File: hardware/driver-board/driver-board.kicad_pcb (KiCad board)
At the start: 4 copper layers, 42.2 x 36.8 mm, 57 parts, among them J1 Conn_01x13_Male, U1 TXS0108E, U2 ME6210, U3 ME6210, U4 TLV61046ADB, U5 NC7SZ125, U6 FT813, U7 ER-TFT040-2, X1 YSX321SL

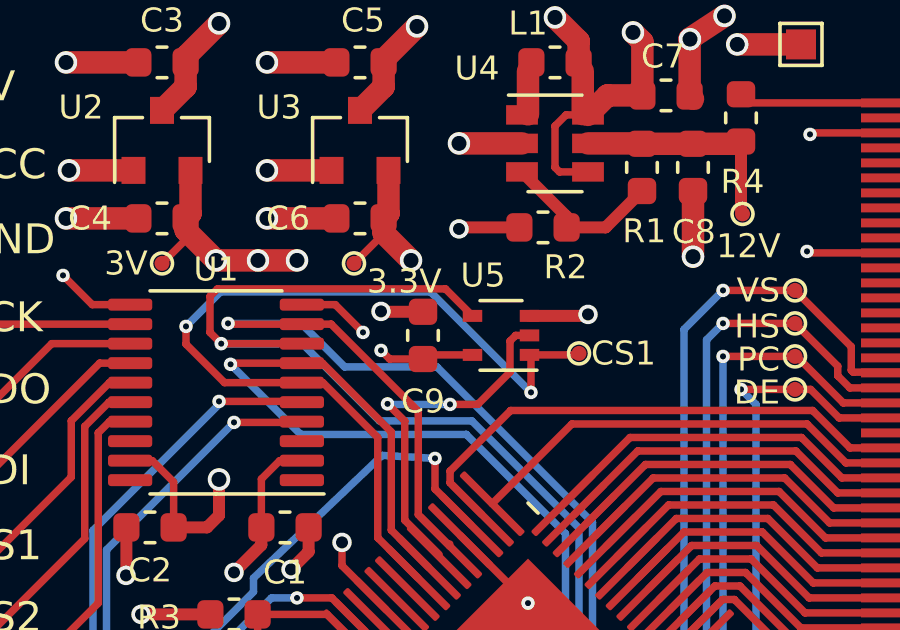
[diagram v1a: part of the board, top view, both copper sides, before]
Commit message: Add drop-in replacement for buffer IC
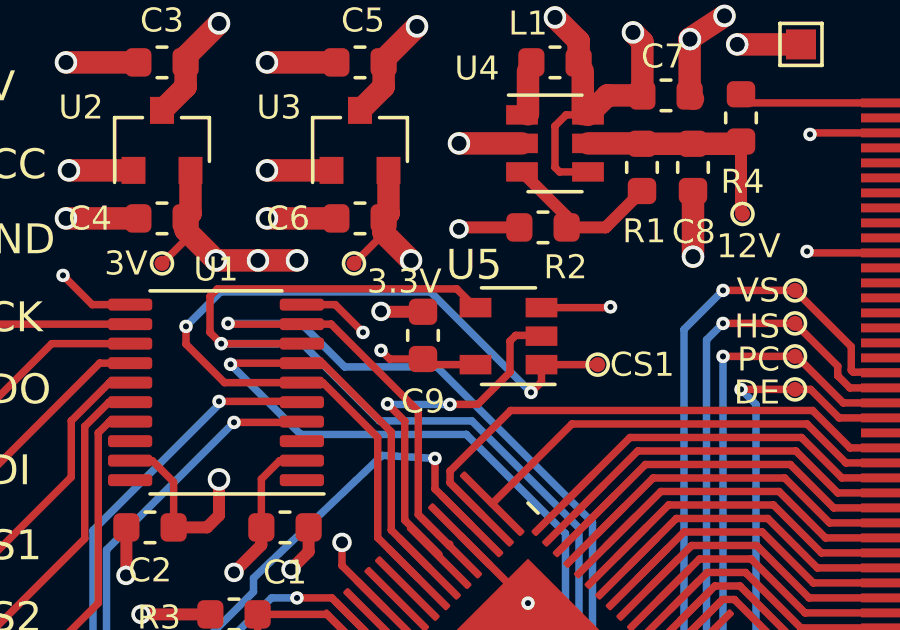
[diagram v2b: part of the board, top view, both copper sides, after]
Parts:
- U5: footprint Package_TO_SOT_SMD:SOT-353_SC-70-5 -> Package_TO_SOT_SMD:SOT-23-5
- moved TP9 0.73 mm to (135.3, 60.4)
- moved U5 0.25 mm to (132.3, 59.4)
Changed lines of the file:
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@@
-    )
-  )
-  (module Package_TO_SOT_SMD:SOT-353_SC-70-5 (layer F.Cu)
-    (at 132.1 59.4 180)
-    (descr "SOT-353, SC-70-5")
-    (tags "SOT-353 SC-70-5")
-    (attr smd)
-    (fp_text reference U5 (at 0.6 2) (layer F.SilkS)
-      (effects (font (size 0.8 0.8) (thickness 0.15)))
-    )
-    (fp_text value NC7SZ125 (at 0 2 180) (layer F.Fab)
-      (effects (font (size 1 1) (thickness 0.15)))
-    )
-    (fp_line (start 0.7 -1.16) (end -1.2 -1.16) (layer F.SilkS) (width 0.12))
-    (fp_line (start -0.7 1.16) (end 0.7 1.16) (layer F.SilkS) (width 0.12))
-    (fp_line (start 1.6 1.4) (end 1.6 -1.4) (layer F.CrtYd) (width 0.05))
-    (fp_line (start -1.6 -1.4) (end -1.6 1.4) (layer F.CrtYd) (width 0.05))
-    (fp_line (start -1.6 -1.4) (end 1.6 -1.4) (layer F.CrtYd) (width 0.05))
-    (fp_line (start 0.675 -1.1) (end -0.175 -1.1) (layer F.Fab) (width 0.1))
-    (fp_line (start -0.675 -0.6) (end -0.675 1.1) (layer F.Fab) (width 0.1))
-    (fp_line (start -1.6 1.4) (end 1.6 1.4) (layer F.CrtYd) (width 0.05))
-    (fp_line (start 0.675 -1.1) (end 0.675 1.1) (layer F.Fab) (width 0.1))
-    (fp_line (start 0.675 1.1) (end -0.675 1.1) (layer F.Fab) (width 0.1))
-    (fp_line (start -0.175 -1.1) (end -0.675 -0.6) (layer F.Fab) (width 0.1))
-    (fp_text user %R (at 0 0 90) (layer F.Fab)
-      (effects (font (size 0.5 0.5) (thickness 0.075)))
-    )
-    (pad 1 smd rect (at -0.95 -0.65 180) (size 0.65 0.4) (layers F.Cu F.Paste F.Mask)
-      (net 20 CS1_3V))
-    (pad 3 smd rect (at -0.95 0.65 180) (size 0.65 0.4) (layers F.Cu F.Paste F.Mask)
-      (net 2 GND))
-    (pad 2 smd rect (at -0.95 0 180) (size 0.65 0.4) (layers F.Cu F.Paste F.Mask)
-      (net 78 SDI_BUFFER))
-    (pad 4 smd rect (at 0.95 0.65 180) (size 0.65 0.4) (layers F.Cu F.Paste F.Mask)
-      (net 76 SDI_3V))
-    (pad 5 smd rect (at 0.95 -0.65 180) (size 0.65 0.4) (layers F.Cu F.Paste F.Mask)
-      (net 1 +3V0))
-    (model ${KISYS3DMOD}/Package_TO_SOT_SMD.3dshapes/SOT-353_SC-70-5.wrl
-      (at (xyz 0 0 0))
-      (scale (xyz 1 1 1))
-      (rotate (xyz 0 0 0))
     )
   )
@@
   )
   (module TestPoint:TestPoint_Pad_D0.5mm (layer F.Cu)
-    (at 134.7 60)
+    (at 135.325 60.375)
     (descr "SMD pad as test Point, diameter 1.0mm")
     (tags "test point SMD pad")
@@
       (net 71 IRQ))
   )
+  (module Package_TO_SOT_SMD:SOT-23-5 (layer F.Cu)
+    (at 132.35 59.425 180)
+    (descr "5-pin SOT23 package")
+    (tags SOT-23-5)
+    (attr smd)
+    (fp_text reference U5 (at 1.15 2.375) (layer F.SilkS)
+      (effects (font (size 1 1) (thickness 0.15)))
+    )
+    (fp_text value NC7SZ125 (at 0 2.9) (layer F.Fab)
+      (effects (font (size 1 1) (thickness 0.15)))
+    )
+    (fp_line (start 0.9 -1.55) (end 0.9 1.55) (layer F.Fab) (width 0.1))
+    (fp_line (start 0.9 1.55) (end -0.9 1.55) (layer F.Fab) (width 0.1))
+    (fp_line (start -0.9 -0.9) (end -0.9 1.55) (layer F.Fab) (width 0.1))
+    (fp_line (start 0.9 -1.55) (end -0.25 -1.55) (layer F.Fab) (width 0.1))
+    (fp_line (start -0.9 -0.9) (end -0.25 -1.55) (layer F.Fab) (width 0.1))
+    (fp_line (start -1.9 1.8) (end -1.9 -1.8) (layer F.CrtYd) (width 0.05))
+    (fp_line (start 1.9 1.8) (end -1.9 1.8) (layer F.CrtYd) (width 0.05))
+    (fp_line (start 1.9 -1.8) (end 1.9 1.8) (layer F.CrtYd) (width 0.05))
+    (fp_line (start -1.9 -1.8) (end 1.9 -1.8) (layer F.CrtYd) (width 0.05))
+    (fp_line (start 0.9 -1.61) (end -1.55 -1.61) (layer F.SilkS) (width 0.12))
+    (fp_line (start -0.9 1.61) (end 0.9 1.61) (layer F.SilkS) (width 0.12))
+    (fp_text user %R (at 0 0 90) (layer F.Fab)
+      (effects (font (size 0.5 0.5) (thickness 0.075)))
+    )
+    (pad 1 smd rect (at -1.1 -0.95 180) (size 1.06 0.65) (layers F.Cu F.Paste F.Mask)
+      (net 20 CS1_3V))
+    (pad 2 smd rect (at -1.1 0 180) (size 1.06 0.65) (layers F.Cu F.Paste F.Mask)
+      (net 78 SDI_BUFFER))
+    (pad 3 smd rect (at -1.1 0.95 180) (size 1.06 0.65) (layers F.Cu F.Paste F.Mask)
+      (net 2 GND))
+    (pad 4 smd rect (at 1.1 0.95 180) (size 1.06 0.65) (layers F.Cu F.Paste F.Mask)
+      (net 76 SDI_3V))
+    (pad 5 smd rect (at 1.1 -0.95 180) (size 1.06 0.65) (layers F.Cu F.Paste F.Mask)
+      (net 1 +3V0))
+    (model ${KISYS3DMOD}/Package_TO_SOT_SMD.3dshapes/SOT-23-5.wrl
+      (at (xyz 0 0 0))
+      (scale (xyz 1 1 1))
+      (rotate (xyz 0 0 0))
+    )
+  )
   (gr_text REV2007D (at 110.5 83.975) (layer F.SilkS)
     (effects (font (size 0.8 0.8) (thickness 0.15) italic) (justify left))
@@
     (effects (font (size 0.8 0.8) (thickness 0.15)))
   )
-  (gr_text CS1 (at 135.1 60) (layer F.SilkS)
+  (gr_text CS1 (at 135.725 60.375) (layer F.SilkS)
     (effects (font (size 0.8 0.8) (thickness 0.15)) (justify left))
   )
@@
   (segment (start 125.4625 63.575) (end 124.725 63.575) (width 0.25) (layer F.Cu) (net 1))
   (segment (start 129.6375 60.05) (end 129.5 60.1875) (width 0.25) (layer F.Cu) (net 1))
-  (segment (start 131.15 60.05) (end 129.6375 60.05) (width 0.25) (layer F.Cu) (net 1))
   (segment (start 143.85 81.15) (end 143.3 81.7) (width 0.4) (layer F.Cu) (net 1))
   (segment (start 143.3 81.7) (end 141.8875 81.7) (width 0.4) (layer F.Cu) (net 1))
@@
   (segment (start 128.3 75.853553) (end 128.3 76.3) (width 0.25) (layer F.Cu) (net 1))
   (segment (start 129.685437 74.468116) (end 128.3 75.853553) (width 0.25) (layer F.Cu) (net 1))
+  (segment (start 129.6875 60.375) (end 129.5 60.1875) (width 0.25) (layer F.Cu) (net 1))
+  (segment (start 131.25 60.375) (end 129.6875 60.375) (width 0.25) (layer F.Cu) (net 1))
   (via (at 123.7 78.6) (size 0.65) (drill 0.4) (layers F.Cu B.Cu) (net 2))
   (segment (start 125.143153 77.156847) (end 123.7 78.6) (width 0.4) (layer F.Cu) (net 2))
@@
   (segment (start 139.6 80.1) (end 138.7 81) (width 0.45) (layer F.Cu) (net 2))
   (segment (start 140.3125 80.1) (end 139.6 80.1) (width 0.45) (layer F.Cu) (net 2))
-  (via (at 135 58.7) (size 0.65) (drill 0.4) (layers F.Cu B.Cu) (net 2))
-  (segment (start 134.95 58.75) (end 135 58.7) (width 0.4) (layer F.Cu) (net 2))
-  (segment (start 133.05 58.75) (end 134.95 58.75) (width 0.4) (layer F.Cu) (net 2))
   (via (at 149.4 52.1) (size 0.45) (drill 0.2) (layers F.Cu B.Cu) (net 2))
   (segment (start 149.35 52.15) (end 149.4 52.1) (width 0.25) (layer F.Cu) (net 2))
@@
   (segment (start 130.75 55.8) (end 130.7 55.85) (width 0.4) (layer F.Cu) (net 2))
   (segment (start 132.7125 55.8) (end 130.75 55.8) (width 0.4) (layer F.Cu) (net 2))
+  (via (at 135.75 58.45) (size 0.45) (drill 0.2) (layers F.Cu B.Cu) (net 2))
+  (segment (start 135.725 58.475) (end 135.75 58.45) (width 0.25) (layer F.Cu) (net 2))
+  (segment (start 133.45 58.475) (end 135.725 58.475) (width 0.25) (layer F.Cu) (net 2))
   (segment (start 121.1875 64.2875) (end 121.1875 65.8) (width 0.25) (layer F.Cu) (net 3))
   (segment (start 120.475 63.575) (end 121.1875 64.2875) (width 0.25) (layer F.Cu) (net 3))
@@
   (segment (start 127.992089 62.802441) (end 127.992089 66.145642) (width 0.25) (layer F.Cu) (net 20))
   (segment (start 125.4625 60.975) (end 126.164648 60.975) (width 0.25) (layer F.Cu) (net 20))
-  (segment (start 134.65 60.05) (end 134.7 60) (width 0.25) (layer F.Cu) (net 20))
-  (segment (start 133.05 60.05) (end 134.65 60.05) (width 0.25) (layer F.Cu) (net 20))
   (segment (start 122.883166 60.975) (end 121.6 59.691834) (width 0.25) (layer F.Cu) (net 20))
   (via (at 121.6 59.1) (size 0.45) (drill 0.2) (layers F.Cu B.Cu) (net 20))
@@
   (segment (start 129.749999 57.949999) (end 133.1 61.3) (width 0.25) (layer B.Cu) (net 20))
   (segment (start 121.6 59.1) (end 122.750001 57.949999) (width 0.25) (layer B.Cu) (net 20))
-  (segment (start 133.1 60.1) (end 133.05 60.05) (width 0.25) (layer F.Cu) (net 20))
-  (segment (start 133.1 61.3) (end 133.1 60.1) (width 0.25) (layer F.Cu) (net 20))
+  (segment (start 133.45 60.95) (end 133.1 61.3) (width 0.25) (layer F.Cu) (net 20))
+  (segment (start 133.45 60.375) (end 133.45 60.95) (width 0.25) (layer F.Cu) (net 20))
+  (segment (start 133.45 60.375) (end 135.325 60.375) (width 0.25) (layer F.Cu) (net 20))
   (segment (start 134.46468 62.35264) (end 142.301231 62.35264) (width 0.25) (layer F.Cu) (net 23))
   (segment (start 143.598591 63.65) (end 145.65 63.65) (width 0.25) (layer F.Cu) (net 23))
@@
   (segment (start 124.773942 59.675) (end 125.4625 59.675) (width 0.25) (layer F.Cu) (net 76))
   (segment (start 122.773952 59.675) (end 125.4625 59.675) (width 0.25) (layer F.Cu) (net 76))
-  (segment (start 122.648962 57.84999) (end 122.4 58.098952) (width 0.25) (layer F.Cu) (net 76))
-  (segment (start 122.4 59.301048) (end 122.773952 59.675) (width 0.25) (layer F.Cu) (net 76))
-  (segment (start 122.4 58.098952) (end 122.4 59.301048) (width 0.25) (layer F.Cu) (net 76))
-  (segment (start 130.24999 57.84999) (end 122.648962 57.84999) (width 0.25) (layer F.Cu) (net 76))
-  (segment (start 131.15 58.75) (end 130.24999 57.84999) (width 0.25) (layer F.Cu) (net 76))
   (via (at 122.773952 59.675) (size 0.45) (drill 0.2) (layers F.Cu B.Cu) (net 76))
   (segment (start 143.864998 77.65) (end 145.65 77.65) (width 0.25) (layer F.Cu) (net 76))
@@
   (segment (start 131.127593 62.250001) (end 134.699989 65.822397) (width 0.25) (layer B.Cu) (net 76))
   (segment (start 122.773952 59.675) (end 125.475 59.675) (width 0.25) (layer B.Cu) (net 76))
+  (segment (start 130.62499 57.84999) (end 131.25 58.475) (width 0.25) (layer F.Cu) (net 76))
+  (segment (start 122.648962 57.84999) (end 130.62499 57.84999) (width 0.25) (layer F.Cu) (net 76))
+  (segment (start 122.4 59.301048) (end 122.4 58.098952) (width 0.25) (layer F.Cu) (net 76))
+  (segment (start 122.4 58.098952) (end 122.648962 57.84999) (width 0.25) (layer F.Cu) (net 76))
+  (segment (start 122.773952 59.675) (end 122.4 59.301048) (width 0.25) (layer F.Cu) (net 76))
   (segment (start 126.151058 60.325) (end 128.442099 62.616041) (width 0.25) (layer F.Cu) (net 77))
   (segment (start 128.442099 62.616041) (end 128.442099 65.888546) (width 0.25) (layer F.Cu) (net 77))
